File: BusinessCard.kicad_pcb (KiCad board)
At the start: 2 copper layers, 88.9 x 50.8 mm, 59 parts, among them J1 RST, J2 USB_B_Micro, SW1 SW_Push, SW10 SW_Push, SW11 SW_Push, SW12 SW_Push, SW13 SW_Push, SW14 SW_Push, SW15 SW_Push, SW16 SW_Push, SW2 SW_Push, SW3 SW_Push, SW4 SW_Push, SW5 SW_Push, SW6 SW_Push, SW7 SW_Push, SW8 SW_Push, SW9 SW_Push, U2 USBLC6-2SC6, U3 ATmega32U4-M, Y1 X322516MLB4SI

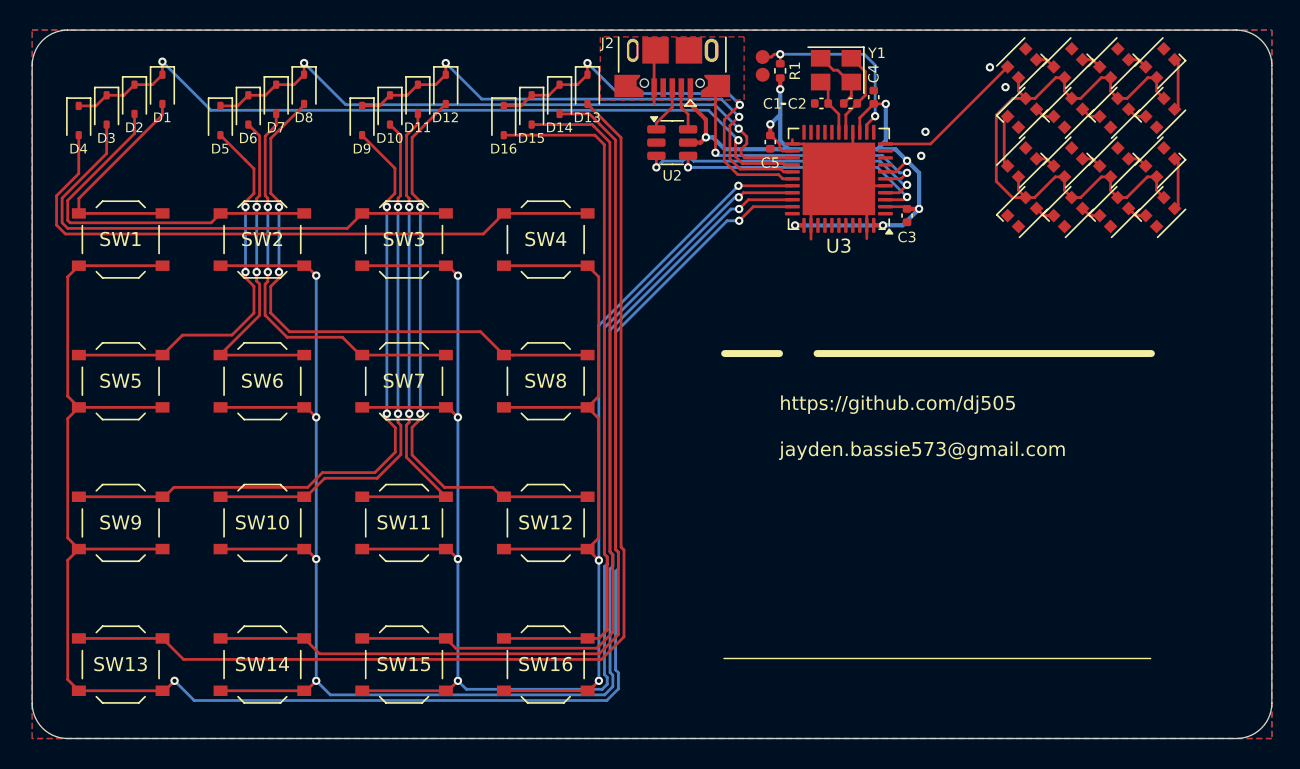
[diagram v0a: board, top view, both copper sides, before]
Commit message: Abusing QR code error correction
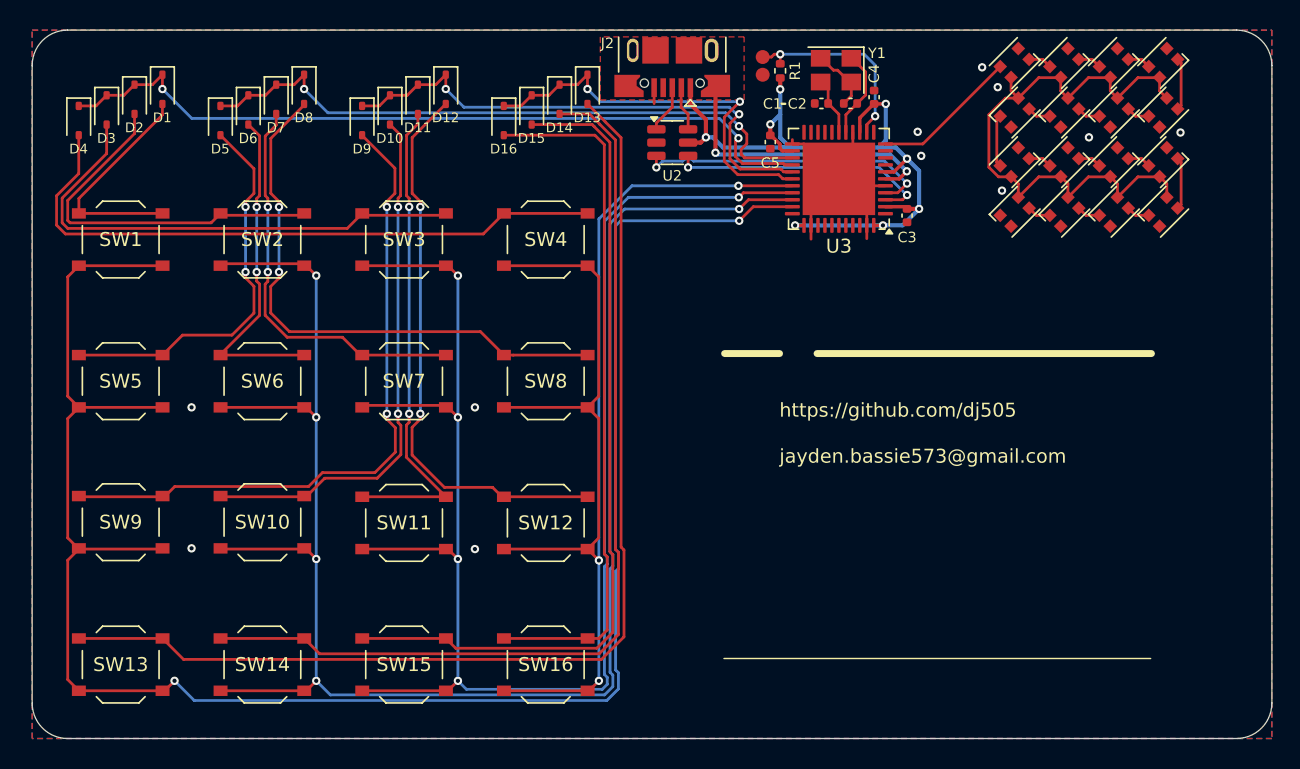
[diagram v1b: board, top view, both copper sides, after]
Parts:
- moved D26 0.53 mm to (193.6, 85.6)
- moved D33 0.53 mm to (193.6, 89.1)
- moved D18 0.53 mm to (193.6, 78.5)
- moved D25 0.53 mm to (193.6, 82.0)
- moved D27 0.27 mm to (197.2, 85.6)
- moved D32 0.27 mm to (197.2, 89.1)
- moved D19 0.27 mm to (197.2, 78.5)
- moved D24 0.27 mm to (197.2, 82.0)
- moved D29 0.21 mm to (204.3, 85.6)
- moved D30 0.21 mm to (204.3, 89.1)
- moved D21 0.21 mm to (204.3, 78.5)
- moved D22 0.21 mm to (204.3, 82.0)
- moved SW10 0.05 mm to (139.7, 111.4)
- moved SW9 0.05 mm to (129.5, 111.4)
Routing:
- net COL3: track 112.1 -> 116.7 mm
- net COL2: track 122.4 -> 127.0 mm
- net COL1: track 132.6 -> 137.1 mm
- net COL4: track 91.4 -> 95.9 mm
- net GND: track 30.8 -> 28.1 mm, vias 4 -> 11
- net ROW1: track 57.1 -> 56.4 mm
- net +5V: track 55.4 -> 56.0 mm
- net RGB: track 11.1 -> 10.5 mm
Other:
- board text added: "Maker, Technician, Developer"
- board text added: "Programmer | Maker | Game Dev Arcade Tech | Graphic Designer"
- board text added: "This card is open source and customizable!"
- board text removed: "Maker & Technician"
- board text removed: "This card is customizable!"

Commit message: Visual changes, alignment fixes, other tweaks
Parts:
- moved D10 0.29 mm to (148.9, 81.6)
- moved D11 0.29 mm to (150.9, 80.8)
- moved D14 0.29 mm to (161.0, 80.8)
- moved D15 0.29 mm to (159.0, 81.6)
- moved D16 0.29 mm to (157.0, 82.3)
- moved D2 0.29 mm to (130.5, 80.8)
- moved D3 0.29 mm to (128.5, 81.6)
- moved D4 0.29 mm to (126.5, 82.3)
- moved D5 0.29 mm to (136.7, 82.3)
- moved D6 0.29 mm to (138.7, 81.6)
- moved D7 0.29 mm to (140.7, 80.8)
- moved D9 0.29 mm to (146.9, 82.3)
- moved D1 0.29 mm to (132.5, 80.1)
- moved D12 0.29 mm to (152.9, 80.1)
- moved D13 0.29 mm to (163.0, 80.1)
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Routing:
- net RGB: track 10.5 -> 12.8 mm
- net GND: vias 11 -> 9
- added copper zone on B.Cu, net (none)
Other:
- board text added: "ATMEGA32U4"
- board text added: "Any Questions?"
- board text added: "By scanning this QR code, you can find... • Extra contact information • Instructions for customization • The bill of materials and KiCAD project files for this card • Assembly instructions • And more!"
- board text added: "KEY MATRIX WITH RGB LIGHTS"
- board text added: "Programmer | Game Dev | Maker Arcade Tech | Graphic Designer"
- board text added: "USB"
- board text added: "WS2812B-2020"
- board text removed: "Jayden Bassie"
- board text removed: "Programmer | Maker | Game Dev Arcade Tech | Graphic Designer"

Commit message: More tweaking, text changes and adjustments
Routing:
- net GND: vias 9 -> 11
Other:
- board text added: "Scan the QR code on the back of the card, or press the highlighted button in a web browser for more info."
- board text added: "This card was made using lead-free solder and RoHS-compliant components."
- board text removed: "Scan the QR code on the back of the card for more info."

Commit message: Updated to the current revision
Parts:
- removed J2: USB_B_Micro, Connector_USB:USB_Micro-B_XKB_U254-051T-4BH83-F1S
- added C6: 1uF, Capacitor_SMD:C_0603_1608Metric, F.Cu at (191.1, 86.6)
- added G***: LOGO, CustomFootprints:HalftoneOverlay, F.Cu at (167.3, 101.7)
- added G***: LOGO, CustomFootprints:HalftoneOverlay, B.Cu at (167.3, 101.2)
- added J3: USB_C_Receptacle_USB2.0_14P, Connector_USB:USB_C_Receptacle_G-Switch_GT-USB-7010ASV, F.Cu at (171.2, 79.8)
- added R2: 22ohm, Resistor_SMD:R_0402_1005Metric, F.Cu at (170.1, 86.0)
- added R3: 22ohm, Resistor_SMD:R_0402_1005Metric, F.Cu at (172.4, 86.0)
- added R4: 5.1k, Resistor_SMD:R_0402_1005Metric, F.Cu at (173.5, 86.0)
- added R5: 5.1k, Resistor_SMD:R_0402_1005Metric, F.Cu at (169.0, 86.0)
- D1, D10, D11, D12, D13, D14, D15, D16, D2, D3, D4, D5, D6, D7, D8, D9: value SOD-123 -> SOD-323
- moved U2 5.14 mm to (171.2, 88.9)
- moved C1 4.04 mm to (183.8, 81.4)
- moved C3 4.04 mm to (190.0, 89.4)
- moved C4 4.04 mm to (187.6, 80.9)
- moved J1 4.04 mm to (179.6, 78.1)
- moved U3 4.04 mm to (185.1, 86.8)
- moved C2 4.04 mm to (185.9, 81.4)
- moved C5 4.04 mm to (180.2, 84.2)
- moved R1 4.04 mm to (180.9, 79.0)
- moved Y1 4.04 mm to (184.9, 79.0)
- moved D19 1.95 mm to (199.2, 78.5)
- moved D21 1.95 mm to (206.3, 78.5)
- moved D22 1.95 mm to (206.3, 82.0)
- moved D24 1.95 mm to (199.2, 82.0)
- moved D27 1.95 mm to (199.2, 85.6)
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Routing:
- net USB_UCAP: track 21.0 -> 3.04 mm, vias 2 -> 0
- net +5V: track 56.0 -> 64.9 mm, vias 8 -> 10
- net Net-(J3-D+-PadA6): track 0.00 -> 4.82 mm
- net ROW1: track 56.6 -> 61.0 mm
- net ROW2: track 46.6 -> 50.8 mm
- net Net-(J3-D--PadA7): track 0.00 -> 4.06 mm
- net ROW4: track 29.5 -> 33.6 mm
- net COL2: track 127.0 -> 131.0 mm
- net COL1: track 137.1 -> 141.1 mm
- net COL3: track 116.7 -> 120.7 mm
- net COL4: track 95.9 -> 99.9 mm
- net ROW3: track 38.3 -> 42.2 mm
- net USB_DP: track 21.6 -> 24.6 mm
- net USB_DN: track 19.1 -> 21.9 mm
- net Net-(J3-CC1): track 0.00 -> 2.37 mm
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- removed copper zone on F.Cu, net USB_UCAP
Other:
- board text added: "// DJ505"
- board text added: "5panel.dance"
- board text added: "Arcade Tech | Graphic Designer"
- board text added: "DESIGNED 2024"
- board text added: "Link icon by SimpleIcon (http://www.simpleicon.com/) via Wikimedia Commons https://creativecommons.org/licenses/by/3.0/"
- board text added: "Maker of Things"
- board text added: "Programmer | Game Dev | Maker"
- board text added: "RST"
- board text added: "SCAN FOR MORE INFO"
- board text added: "[REDACTED]"
- board text added: "business@5panel.dance"
- board text added: "•••"
- board text removed: "Any Questions?"
- board text removed: "By scanning this QR code, you can find... • Extra contact information • Instructions for customization • The bill of materials and KiCAD project files for this card • Assembly instructions • And more!"
- board text removed: "Maker, Technician, Developer"
- board text removed: "Programmer | Game Dev | Maker Arcade Tech | Graphic Designer"
- board text removed: "This card was made using lead-free solder and RoHS-compliant components."
- board text removed: "https://github.com/dj505"
- board text removed: "jayden.bassie573@gmail.com"

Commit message: Update
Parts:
- added REF**: MountingHole_ToolingHole_1.152mm, MountingHole:MountingHole_ToolingHole_1.152mm, F.Cu at (210.1, 78.1)
- added REF**: MountingHole_ToolingHole_1.152mm, MountingHole:MountingHole_ToolingHole_1.152mm, F.Cu at (125.2, 124.9)
- moved U2 0.32 mm to (171.2, 89.2), turned to -90 degrees
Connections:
- D18 pad 4: Net-(D18-VDD) -> +5V
- D19 pad 4: Net-(D18-VDD) -> +5V
- D20 pad 4: Net-(D18-VDD) -> +5V
- D21 pad 4: Net-(D18-VDD) -> +5V
- D22 pad 4: Net-(D18-VDD) -> +5V
- D23 pad 4: Net-(D18-VDD) -> +5V
- D24 pad 4: Net-(D18-VDD) -> +5V
- D25 pad 4: Net-(D18-VDD) -> +5V
- D26 pad 4: Net-(D18-VDD) -> +5V
- D27 pad 4: Net-(D18-VDD) -> +5V
- D28 pad 4: Net-(D18-VDD) -> +5V
- D29 pad 4: Net-(D18-VDD) -> +5V
- D30 pad 4: Net-(D18-VDD) -> +5V
- D31 pad 4: Net-(D18-VDD) -> +5V
- D32 pad 4: Net-(D18-VDD) -> +5V
- D33 pad 4: Net-(D18-VDD) -> +5V
- U2 pad 3: USB_DP -> USBLC6_DN
- U2 pad 6: USBLC6_DN -> USB_DP
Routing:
- net +5V: track 64.9 -> 112.0 mm, vias 10 -> 11
- net Net-(D18-VDD): track 43.7 -> 0.00 mm
- net USBLC6_DP: track 1.38 -> 0.00 mm
- net USBLC6_DN: track 1.38 -> 0.00 mm
- net USB_DP: track 24.6 -> 23.5 mm, vias 2 -> 1
- net USB_DN: track 21.9 -> 20.7 mm, vias 2 -> 1
- net Net-(J3-D--PadA7): track 4.06 -> 4.99 mm
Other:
- board text added: "Scan the QR code on the back of the card, or visit 5panel.dance/BusinessCard for more information."
- board text removed: "Scan the QR code on the back of the card, or press the highlighted button in a web browser for more info."
